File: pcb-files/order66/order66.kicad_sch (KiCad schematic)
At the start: 144 parts, among them J1 NICEVIEW, J2 Pouch Battery Connector, SW1 AUX1, SW10 Z, SW11 AUX7, SW12 2, SW13 W, SW14 S, SW15 X, SW16 LALT, SW17 3, SW18 E, SW19 D, SW2 ESC, SW20 C, SW21 GUI, SW22 4, SW23 R, SW24 F, SW25 V, SW26 RAISE, SW27 5, SW28 T, SW29 G, SW3 TAB, SW30 B, SW31 LSPACE, SW32 AUX2, SW33 6, SW34 Y, SW35 H, SW36 N, SW37 RSPACE, SW38 AUX3, SW39 7, SW4 CAPSLCK, SW40 U, SW41 J, SW42 M, SW43 LOWER, SW44 AUX4, SW45 8, SW46 I, SW47 K, SW48 ,<, SW49 LEFT, SW5 LSHIFT, SW50 9, SW51 O, SW52 L, SW53 .>, SW54 DOWN, SW55 AUX5, SW56 0, SW57 P, SW58 ;:, SW59 /?, SW6 LCTRL, SW60 UP, SW61 AUX6, SW62 BACKSPACE, SW63 BACKSLACH, SW64 ENTER, SW65 RSHIFT, SW66 RIGHT, SW67 RST, SW68 ON/OFF, SW7 1, SW8 Q, SW9 A, U1 NiceNano

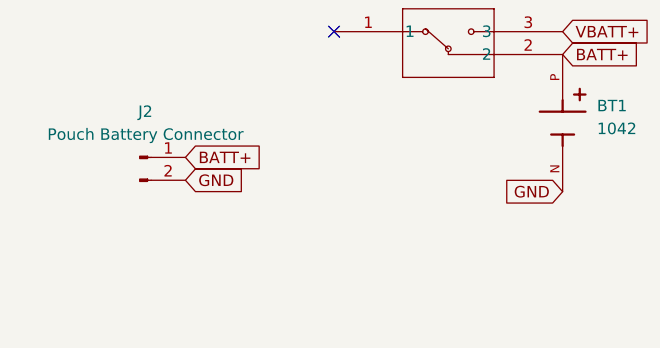
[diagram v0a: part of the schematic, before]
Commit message: added support for millmax spring loaded swd pins for bootloader support
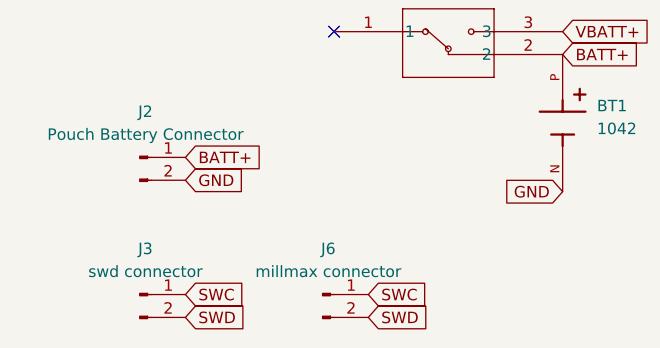
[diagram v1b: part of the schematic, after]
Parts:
- added J3: swd connector, Connector_PinHeader_2.54mm:PinHeader_1x02_P2.54mm_Horizontal, symbol Connector:Conn_01x02_Pin
- added J6: millmax connector, Connector_PinHeader_2.54mm:PinHeader_1x02_P2.54mm_Vertical, symbol Connector:Conn_01x02_Pin
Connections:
- new net SWC: J3.1 (Pin_1), J6.1 (Pin_1)
- new net SWD: J3.2 (Pin_2), J6.2 (Pin_2)
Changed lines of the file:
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@@
 		)
 	)
+	(global_label "SWC"
+		(shape input)
+		(at 59.69 173.99 0)
+		(fields_autoplaced yes)
+		(effects
+			(font
+				(size 1.27 1.27)
+			)
+			(justify left)
+		)
+		(property "Intersheetrefs" "${INTERSHEET_REFS}"
+			(at 66.6061 173.99 0)
+			(effects
+				(font
+					(size 1.27 1.27)
+				)
+				(justify left)
+				(hide yes)
+			)
+		)
+	)
 	(global_label "RST"
 		(shape input)
@@
 		)
 	)
+	(global_label "SWC"
+		(shape input)
+		(at 39.37 173.99 0)
+		(fields_autoplaced yes)
+		(effects
+			(font
+				(size 1.27 1.27)
+			)
+			(justify left)
+		)
+		(property "Intersheetrefs" "${INTERSHEET_REFS}"
+			(at 46.2861 173.99 0)
+			(effects
+				(font
+					(size 1.27 1.27)
+				)
+				(justify left)
+				(hide yes)
+			)
+		)
+	)
 	(global_label "COL9"
 		(shape input)
@@
 		)
 	)
+	(global_label "SWD"
+		(shape input)
+		(at 59.69 176.53 0)
+		(fields_autoplaced yes)
+		(effects
+			(font
+				(size 1.27 1.27)
+			)
+			(justify left)
+		)
+		(property "Intersheetrefs" "${INTERSHEET_REFS}"
+			(at 66.6061 176.53 0)
+			(effects
+				(font
+					(size 1.27 1.27)
+				)
+				(justify left)
+				(hide yes)
+			)
+		)
+	)
 	(global_label "RST"
 		(shape input)
@@
 		)
 	)
+	(global_label "SWD"
+		(shape input)
+		(at 39.37 176.53 0)
+		(fields_autoplaced yes)
+		(effects
+			(font
+				(size 1.27 1.27)
+			)
+			(justify left)
+		)
+		(property "Intersheetrefs" "${INTERSHEET_REFS}"
+			(at 46.2861 176.53 0)
+			(effects
+				(font
+					(size 1.27 1.27)
+				)
+				(justify left)
+				(hide yes)
+			)
+		)
+	)
 	(global_label "COL10"
 		(shape input)
@@
 	)
 	(symbol
+		(lib_id "Connector:Conn_01x02_Pin")
+		(at 34.29 173.99 0)
+		(unit 1)
+		(exclude_from_sim no)
+		(in_bom yes)
+		(on_board yes)
+		(dnp no)
+		(fields_autoplaced yes)
+		(property "Reference" "J3"
+			(at 34.925 168.91 0)
+			(effects
+				(font
+					(size 1.27 1.27)
+				)
+			)
+		)
+		(property "Value" "swd connector"
+			(at 34.925 171.45 0)
+			(effects
+				(font
+					(size 1.27 1.27)
+				)
+			)
+		)
+		(property "Footprint" "Connector_PinHeader_2.54mm:PinHeader_1x02_P2.54mm_Horizontal"
+			(at 34.29 173.99 0)
+			(effects
+				(font
+					(size 1.27 1.27)
+				)
+				(hide yes)
+			)
+		)
+		(property "Datasheet" "~"
+			(at 34.29 173.99 0)
+			(effects
+				(font
+					(size 1.27 1.27)
+				)
+				(hide yes)
+			)
+		)
+		(property "Description" "Generic connector, single row, 01x02, script generated"
+			(at 34.29 173.99 0)
+			(effects
+				(font
+					(size 1.27 1.27)
+				)
+				(hide yes)
+			)
+		)
+		(pin "1"
+		)
+		(pin "2"
+		)
+		(instances
+			(project ""
+				(path "/4342f055-467b-4789-a8ed-b19f1b214d4d"
+					(reference "J3")
+					(unit 1)
+				)
+			)
+		)
+	)
+	(symbol
 		(lib_id "Switch:SW_Push")
 		(at 238.76 106.68 0)
@@
 					(unit 1)
 				)
+			)
+		)
+	)
+	(symbol
+		(lib_id "Connector:Conn_01x02_Pin")
+		(at 54.61 173.99 0)
+		(unit 1)
+		(exclude_from_sim no)
+		(in_bom yes)
+		(on_board yes)
+		(dnp no)
+		(fields_autoplaced yes)
+		(property "Reference" "J6"
+			(at 55.245 168.91 0)
+			(effects
+				(font
+					(size 1.27 1.27)
+				)
+			)
+		)
+		(property "Value" "millmax connector"
+			(at 55.245 171.45 0)
+			(effects
+				(font
+					(size 1.27 1.27)
+				)
+			)
+		)
+		(property "Footprint" "Connector_PinHeader_2.54mm:PinHeader_1x02_P2.54mm_Vertical"
+			(at 54.61 173.99 0)
+			(effects
+				(font
+					(size 1.27 1.27)
+				)
+				(hide yes)
+			)
+		)
+		(property "Datasheet" "~"
+			(at 54.61 173.99 0)
+			(effects
+				(font
+					(size 1.27 1.27)
+				)
+				(hide yes)
+			)
+		)
+		(property "Description" "Generic connector, single row, 01x02, script generated"
+			(at 54.61 173.99 0)
+			(effects
+				(font
+					(size 1.27 1.27)
+				)
+				(hide yes)
+			)
+		)
+		(pin "1"
+		)
+		(pin "2"
+		)
+		(instances
+			(project "order66"
+				(path "/4342f055-467b-4789-a8ed-b19f1b214d4d"
+					(reference "J6")
+					(unit 1)
+				)
